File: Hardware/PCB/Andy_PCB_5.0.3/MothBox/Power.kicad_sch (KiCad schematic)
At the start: 42 parts, among them J1 DB141V-2.54-4P, J2 DB141V-2.54-4P, J3 DB141V-2.54-4P, Q1 JMTV210P02A, Q2 AO3400A, Q8 JMTV210P02A, SW2 KH-6X6X5H-STM, U1 Place Holder voltage regulator, U2 XL4015E1, U3 INA219BIDCNT

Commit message: version 5.0.3 completed changes, as per CHANGELOG
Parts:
- added D2, D4: 6.8V, MothBox_footprints_Library:D_SOD-323, symbol MothBox_Symbol_Library:D_Zener_Small
- added JP2: Jumper_2_Small_Bridged, symbol Jumper:Jumper_2_Small_Bridged
- added Q10: JMTV210P02A, MothBox_footprints_Library:U-DFN2020-6_L2.0-W2.0-P0.65-BL, symbol MothBox_Symbol_Library:JMTV210P02A
- added R38, R40, R41: 4.7K, MothBox_footprints_Library:R_0603_1608Metric, symbol MothBox_Symbol_Library:R_Small
- added R39: 10K, MothBox_footprints_Library:R_0603_1608Metric, symbol MothBox_Symbol_Library:R_Small
- D1: value 10V -> 6.8V; DESCRIPTION (none) -> BZT52C6V8S; LCSC_Part C571388 -> C46641604
- F2: value 6A trip -> 7A trip; footprint Fuse:Fuse_1812_4532Metric -> Fuse:Fuse_2920_7451Metric; LCSC_Part C7500481 -> C22363536
- R4: value 0.1R/1% -> 0.033R/1%; LCSC_Part C23067426 -> C875726
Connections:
- net +12V: now also D2.1 (K), Q10.4 (S), Q10.7 (S); no longer J1.3 (Pin_3), J1.4 (Pin_4), U1.4 (Vout+)
- net +24V: now also D4.1 (K), JP2.2 (B); no longer R30.1
- net GND: now also R38.2, R40.2, R41.1; no longer R29.2
- net at F2.2, R4.2, U3.1 (IN+): now also JP2.1 (A)
- net at Q2.3 (D), Q8.3 (G): no longer R30.2
- new net: R39.2, R40.1
- new net: R29.2, R38.1
- new net: D4.2 (A), R30.2
- new net: D2.2 (A), Q10.3 (G), R39.1
- new net: J1.3 (Pin_3), J1.4 (Pin_4), Q10.1 (D), Q10.2 (D), Q10.5 (D), Q10.6 (D), Q10.8 (D), U1.4 (Vout+)
- new net: R30.1, R41.2
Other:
- note added: "2920 size"
- note added: "Cut Jumper to measure current flow"
- note added: "INA219 Current Sensor Bypass"
- note added: "Switch the External Regulator on and Off"
- note added: "To External 12V Regulator"
- note removed: "Switch the Regulator on and Off"
- moved on the sheet: D1, J1, Q2, R1, R29, R30, TP5

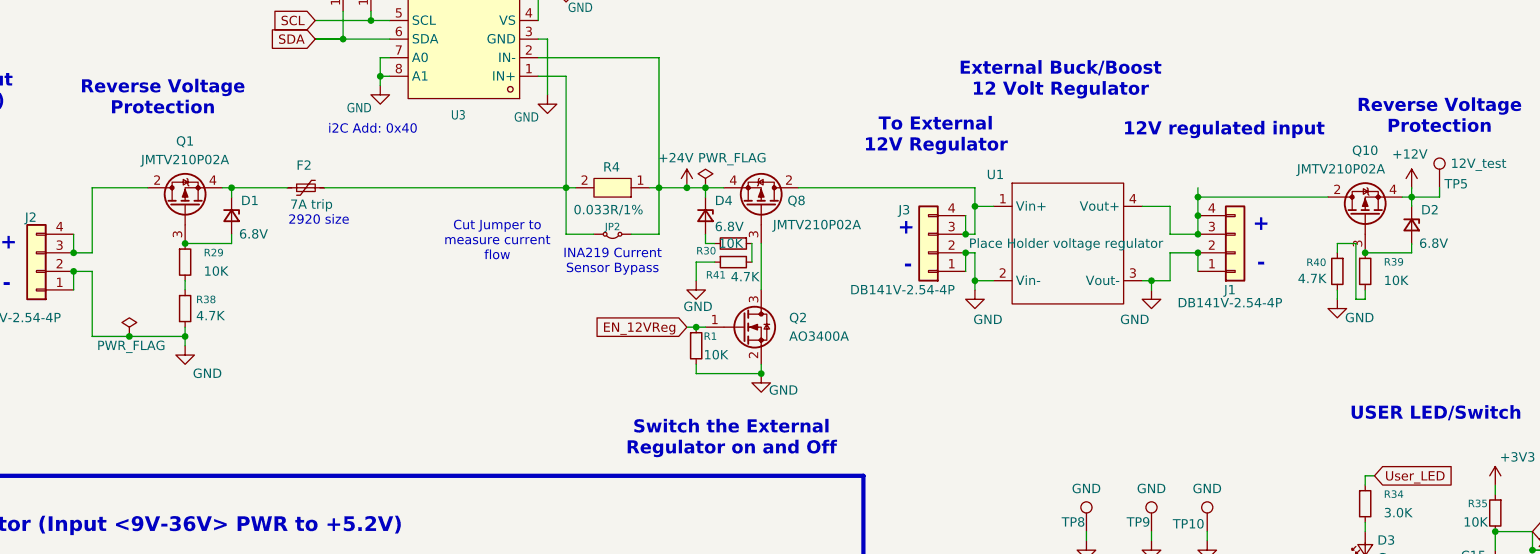
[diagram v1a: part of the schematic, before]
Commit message: swapped out Q1, Q8, Q10 for better specc'ed MOSFETs. Moved a few tracks around and updated CHANGELOG.txt
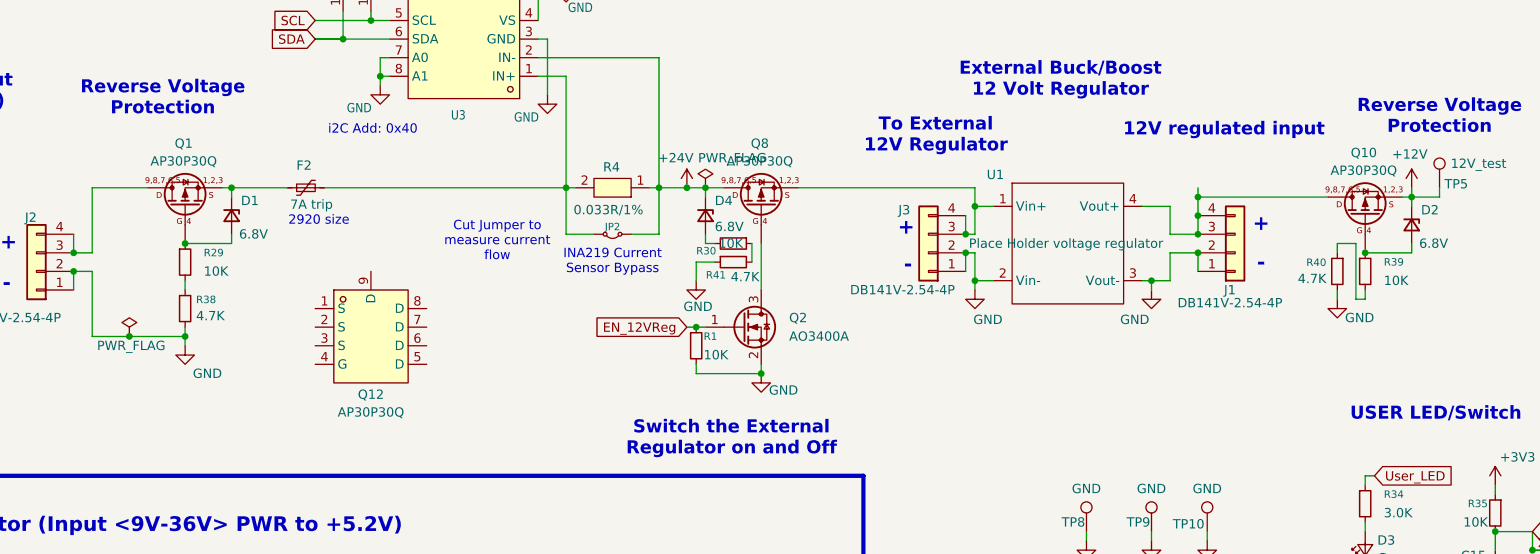
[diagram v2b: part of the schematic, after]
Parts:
- removed Q1, Q10, Q8: JMTV210P02A, MothBox_footprints_Library:U-DFN2020-6_L2.0-W2.0-P0.65-BL, symbol MothBox_Symbol_Library:JMTV210P02A
- added Q1, Q10, Q8: AP30P30Q, 0_easyeda_footprints:PDFN3333-8_L3.1-W3.2-P0.65-LS3.4-BL, symbol MothBox_Symbol_Library:AP30P30Q_1
- added Q12: AP30P30Q, easyeda2kicad:PDFN3333-8_L3.1-W3.2-P0.65-LS3.4-BL, symbol MothBox_Symbol_Library:AP30P30Q
- D3: symbol 0_pauls_symbols:Device_LED_Small -> MothBox_Symbol_Library:Device_LED_Small
- JP2: symbol Jumper:Jumper_2_Small_Bridged -> MothBox_Symbol_Library:Jumper_2_Small_Bridged
- Q2: symbol Transistor_FET:AO3400A -> MothBox_Symbol_Library:AO3400A
- SW2: symbol 0_easyeda2kicad:KH-6X6X5H-STM -> MothBox_Symbol_Library:KH-6X6X5H-STM
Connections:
- net +12V: now also Q10.1 (S), Q10.2 (S), Q10.3 (S)
- net +24V: now also Q8.5 (D), Q8.6 (D), Q8.7 (D), Q8.8 (D), Q8.9 (D)
- net at J3.3 (Pin_3), J3.4 (Pin_4), U1.1 (Vin+): now also Q8.1 (S), Q8.2 (S), Q8.3 (S)
- net at D1.1 (K), F2.1: now also Q1.1 (S), Q1.2 (S), Q1.3 (S)
- net at J2.3 (Pin_3), J2.4 (Pin_4): now also Q1.5 (D), Q1.6 (D), Q1.7 (D), Q1.8 (D), Q1.9 (D)
- net at D2.2 (A), R39.1: now also Q10.4 (G)
- net at D1.2 (A), R29.1: now also Q1.4 (G)
- net at J1.3 (Pin_3), J1.4 (Pin_4), U1.4 (Vout+): now also Q10.5 (D), Q10.6 (D), Q10.7 (D), Q10.8 (D), Q10.9 (D)
- net at Q2.3 (D): now also Q8.4 (G)

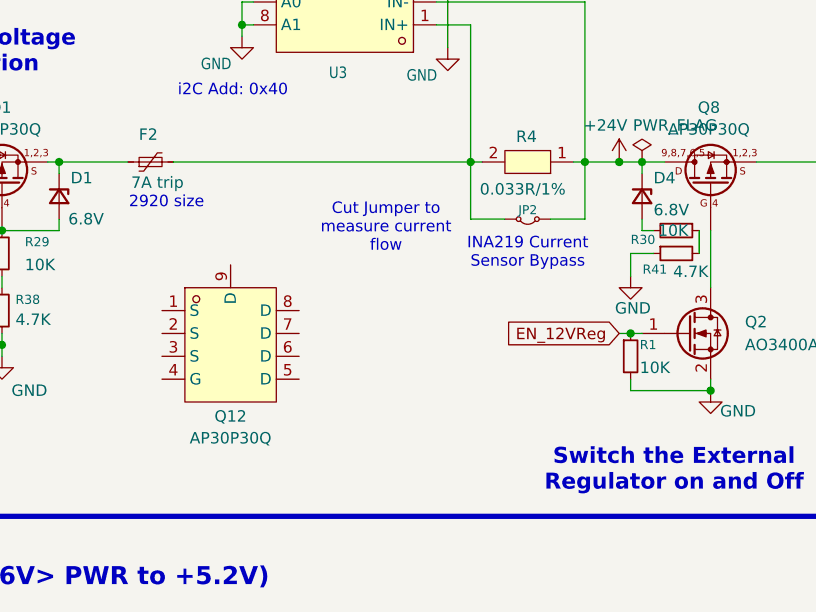
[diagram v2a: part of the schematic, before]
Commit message: Passes DRC - updated cuttable jumper, updated 3v3 mosfet, updated holes for battery
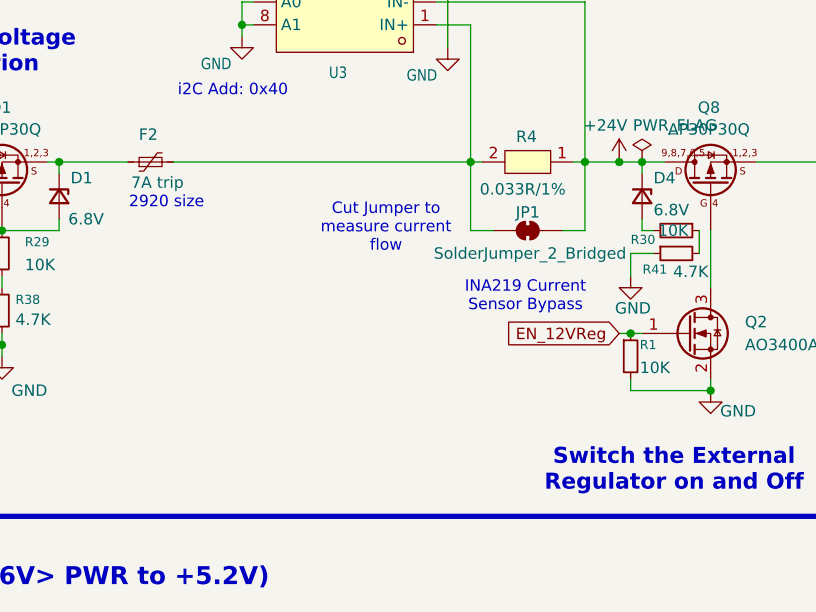
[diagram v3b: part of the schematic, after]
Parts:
- removed JP2: Jumper_2_Small_Bridged, symbol MothBox_Symbol_Library:Jumper_2_Small_Bridged
- removed Q12: AP30P30Q, easyeda2kicad:PDFN3333-8_L3.1-W3.2-P0.65-LS3.4-BL, symbol MothBox_Symbol_Library:AP30P30Q
- added JP1: SolderJumper_2_Bridged, Jumper:SolderJumper-2_P1.3mm_Bridged2Bar_RoundedPad1.0x1.5mm, symbol Jumper:SolderJumper_2_Bridged
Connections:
- net +24V: now also JP1.2 (B)
- net at F2.2, R4.2, U3.1 (IN+): now also JP1.1 (A)
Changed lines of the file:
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@@
 	(text "INA219 Current\nSensor Bypass"
 		(exclude_from_sim no)
-		(at 137.16 85.09 0)
+		(at 136.906 89.916 0)
 		(effects
 			(font
@@
 	(wire
 		(pts
+			(xy 133.35 82.55) (xy 130.81 82.55)
+		)
+		(stroke
+			(width 0)
+			(type default)
+		)
+	)
+	(wire
+		(pts
 			(xy 151.13 137.16) (xy 151.13 138.43)
 		)
@@
 	(wire
 		(pts
-			(xy 130.81 81.28) (xy 130.81 74.93)
+			(xy 130.81 82.55) (xy 130.81 74.93)
 		)
 		(stroke
@@
 	(wire
 		(pts
-			(xy 143.51 81.28) (xy 143.51 74.93)
+			(xy 143.51 82.55) (xy 143.51 74.93)
 		)
 		(stroke
@@
 	(wire
 		(pts
-			(xy 240.03 88.9) (xy 240.03 90.17)
+			(xy 140.97 82.55) (xy 143.51 82.55)
 		)
 		(stroke
@@
 	(wire
 		(pts
-			(xy 257.81 121.92) (xy 257.81 124.46)
+			(xy 240.03 88.9) (xy 240.03 90.17)
 		)
 		(stroke
@@
 	(wire
 		(pts
-			(xy 100.33 138.43) (xy 106.68 138.43)
+			(xy 257.81 121.92) (xy 257.81 124.46)
 		)
 		(stroke
@@
 	(wire
 		(pts
-			(xy 134.62 152.4) (xy 134.62 157.48)
+			(xy 100.33 138.43) (xy 106.68 138.43)
 		)
 		(stroke
@@
 	(wire
 		(pts
-			(xy 154.94 143.51) (xy 154.94 138.43)
+			(xy 134.62 152.4) (xy 134.62 157.48)
 		)
 		(stroke
@@
 	(wire
 		(pts
-			(xy 154.94 152.4) (xy 147.32 152.4)
+			(xy 154.94 143.51) (xy 154.94 138.43)
 		)
 		(stroke
@@
 	(wire
 		(pts
-			(xy 262.89 124.46) (xy 273.05 124.46)
+			(xy 154.94 152.4) (xy 147.32 152.4)
 		)
 		(stroke
@@
 	(wire
 		(pts
-			(xy 139.7 81.28) (xy 143.51 81.28)
+			(xy 262.89 124.46) (xy 273.05 124.46)
 		)
 		(stroke
@@
 	(wire
 		(pts
-			(xy 134.62 81.28) (xy 130.81 81.28)
-		)
-		(stroke
-			(width 0)
-			(type default)
-		)
-	)
-	(wire
-		(pts
 			(xy 257.81 129.54) (xy 257.81 132.08)
 		)
@@
 	)
 	(symbol
-		(lib_id "MothBox_Symbol_Library:Jumper_2_Small_Bridged")
-		(at 137.16 81.28 0)
-		(mirror x)
-		(unit 1)
-		(exclude_from_sim no)
-		(in_bom yes)
-		(on_board yes)
-		(dnp no)
-		(property "Reference" "JP2"
-			(at 137.16 80.264 0)
-			(effects
-				(font
-					(size 1 1)
-				)
-			)
-		)
-		(property "Value" "Jumper_2_Small_Bridged"
-			(at 137.16 83.4428 0)
-			(effects
-				(font
-					(size 1.27 1.27)
-				)
-				(hide yes)
-			)
-		)
-		(property "Footprint" ""
-			(at 137.16 81.28 0)
-			(effects
-				(font
-					(size 1.27 1.27)
-				)
-				(hide yes)
-			)
-		)
-		(property "Datasheet" "~"
-			(at 137.16 81.28 0)
-			(effects
-				(font
-					(size 1.27 1.27)
-				)
-				(hide yes)
-			)
-		)
-		(property "Description" "Jumper, 2-pole, small symbol, bridged"
-			(at 137.16 81.28 0)
-			(effects
-				(font
-					(size 1.27 1.27)
-				)
-				(hide yes)
-			)
-		)
-		(pin "2"
-		)
-		(pin "1"
-		)
-		(instances
-			(project ""
-				(path "/9021e528-fc76-4423-a3f3-30f5652071cc/4a573100-9946-48c2-8ae5-35f893607623"
-					(reference "JP2")
-					(unit 1)
-				)
-			)
-		)
-	)
-	(symbol
 		(lib_id "MothBox_Symbol_Library:GND")
 		(at 128.27 62.23 0)
@@
 	)
 	(symbol
+		(lib_id "Jumper:SolderJumper_2_Bridged")
+		(at 137.16 82.55 0)
+		(unit 1)
+		(exclude_from_sim no)
+		(in_bom no)
+		(on_board yes)
+		(dnp no)
+		(property "Reference" "JP1"
+			(at 137.16 80.518 0)
+			(effects
+				(font
+					(size 1.27 1.27)
+				)
+			)
+		)
+		(property "Value" "SolderJumper_2_Bridged"
+			(at 137.414 85.09 0)
+			(effects
+				(font
+					(size 1.27 1.27)
+				)
+			)
+		)
+		(property "Footprint" "Jumper:SolderJumper-2_P1.3mm_Bridged2Bar_RoundedPad1.0x1.5mm"
+			(at 137.16 82.55 0)
+			(effects
+				(font
+					(size 1.27 1.27)
+				)
+				(hide yes)
+			)
+		)
+		(property "Datasheet" "~"
+			(at 137.16 82.55 0)
+			(effects
+				(font
+					(size 1.27 1.27)
+				)
+				(hide yes)
+			)
+		)
+		(property "Description" "Solder Jumper, 2-pole, closed/bridged"
+			(at 137.16 82.55 0)
+			(effects
+				(font
+					(size 1.27 1.27)
+				)
+				(hide yes)
+			)
+		)
+		(pin "1"
+		)
+		(pin "2"
+		)
+		(instances
+			(project ""
+				(path "/9021e528-fc76-4423-a3f3-30f5652071cc/4a573100-9946-48c2-8ae5-35f893607623"
+					(reference "JP1")
+					(unit 1)
+				)
+			)
+		)
+	)
+	(symbol
 		(lib_id "MothBox_Symbol_Library:R_Small")
 		(at 78.74 91.44 0)
@@
 					(unit 1)
 				)
-			)
-		)
-	)
-	(symbol
-		(lib_id "MothBox_Symbol_Library:AP30P30Q")
-		(at 104.14 95.25 0)
-		(unit 1)
-		(exclude_from_sim no)
-		(in_bom yes)
-		(on_board yes)
-		(dnp no)
-		(fields_autoplaced yes)
-		(property "Reference" "Q12"
-			(at 104.14 103.1931 0)
-			(effects
-				(font
-					(size 1.27 1.27)
-				)
-			)
-		)
-		(property "Value" "AP30P30Q"
-			(at 104.14 105.6174 0)
-			(effects
-				(font
-					(size 1.27 1.27)
-				)
-			)
-		)
-		(property "Footprint" "easyeda2kicad:PDFN3333-8_L3.1-W3.2-P0.65-LS3.4-BL"
-			(at 104.14 106.68 0)
-			(effects
-				(font
-					(size 1.27 1.27)
-				)
-				(hide yes)
-			)
-		)
-		(property "Datasheet" ""
-			(at 104.14 95.25 0)
-			(effects
-				(font
-					(size 1.27 1.27)
-				)
-				(hide yes)
-			)
-		)
-		(property "Description" ""
-			(at 104.14 95.25 0)
-			(effects
-				(font
-					(size 1.27 1.27)
-				)
-				(hide yes)
-			)
-		)
-		(property "LCSC Part" "C471913"
-			(at 104.14 109.22 0)
-			(effects
-				(font
-					(size 1.27 1.27)
-				)
-				(hide yes)
-			)
-		)
-		(pin "8"
-		)
-		(pin "6"
-		)
-		(pin "2"
-		)
-		(pin "7"
-		)
-		(pin "9"
-		)
-		(pin "4"
-		)
-		(pin "3"
-		)
-		(pin "1"
-		)
-		(pin "5"
-		)
-		(instances
-			(project ""
-				(path "/9021e528-fc76-4423-a3f3-30f5652071cc/4a573100-9946-48c2-8ae5-35f893607623"
-					(reference "Q12")
-					(unit 1)
-				)

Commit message: Fixed big capacitor library footprint
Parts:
- C14, C16: footprint 0_easyeda_footprints:CAP-TH_BD16.0-P7.50-D1.2-FD -> easyeda2kicad:CAP-TH_BD16.0-P7.50-D1.2-FD
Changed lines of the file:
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@@
 			)
 		)
-		(property "Footprint" "0_easyeda_footprints:CAP-TH_BD16.0-P7.50-D1.2-FD"
+		(property "Footprint" "easyeda2kicad:CAP-TH_BD16.0-P7.50-D1.2-FD"
 			(at 134.62 146.05 0)
 			(effects
@@
 			)
 		)
-		(property "Footprint" "0_easyeda_footprints:CAP-TH_BD16.0-P7.50-D1.2-FD"
+		(property "Footprint" "easyeda2kicad:CAP-TH_BD16.0-P7.50-D1.2-FD"
 			(at 49.53 143.51 0)
 			(effects
@@
 			)
 		)
-		(property "Datasheet" "https://lcsc.com/product-detail/Aluminum-Electrolytic-Capacitors-Leaded_1000uF-20-50V_C106656.html"
+		(property "Datasheet" "~"
 			(at 49.53 143.51 0)
 			(effects
@@
 			)
 		)
-		(property "Description" ""
+		(property "Description" "Polarized capacitor, small US symbol"
 			(at 49.53 143.51 0)
 			(effects

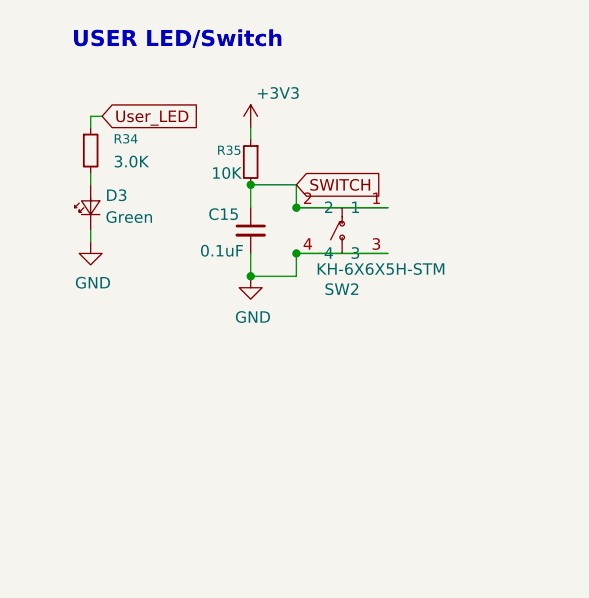
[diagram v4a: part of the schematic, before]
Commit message: Had to swap SW2 for a SMD version
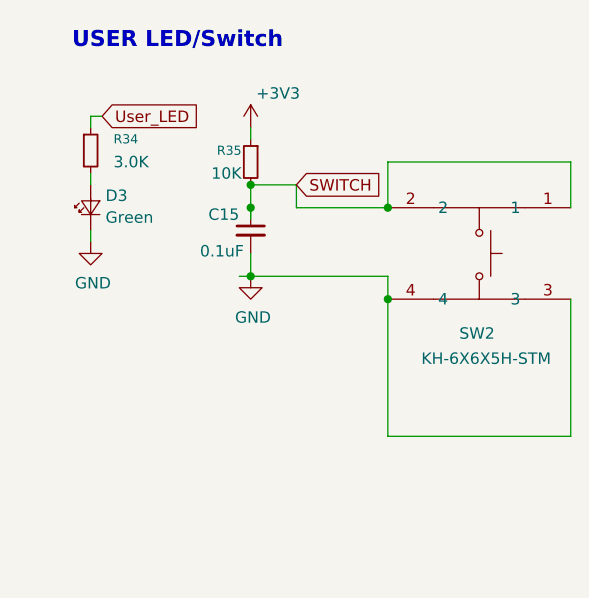
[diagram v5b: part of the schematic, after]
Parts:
- SW2: footprint 0_easyeda_footprints:SW-SMD_4P-L6.0-W6.0-P4.50-LS9.0_H5.0 -> easyeda2kicad:KEY-SMD_4P-L6.0-W6.0-P4.50-LS10.0-TL; symbol MothBox_Symbol_Library:KH-6X6X5H-STM -> easyeda2kicad:4-1437565-1; LCSC Part C455095 -> C592734
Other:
- moved on the sheet: SW2
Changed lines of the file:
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@@
 	)
 	(junction
+		(at 257.81 124.46)
+		(diameter 0)
+		(color 0 0 0 0)
+	)
+	(junction
 		(at 100.33 54.61)
 		(diameter 0)
@@
 	)
 	(junction
-		(at 186.69 87.63)
+		(at 273.05 134.62)
 		(diameter 0)
 		(color 0 0 0 0)
 	)
 	(junction
-		(at 63.5 86.36)
+		(at 186.69 87.63)
 		(diameter 0)
 		(color 0 0 0 0)
 	)
 	(junction
-		(at 134.62 138.43)
+		(at 63.5 86.36)
 		(diameter 0)
 		(color 0 0 0 0)
 	)
 	(junction
-		(at 154.94 138.43)
+		(at 134.62 138.43)
 		(diameter 0)
 		(color 0 0 0 0)
 	)
 	(junction
-		(at 262.89 124.46)
+		(at 154.94 138.43)
 		(diameter 0)
 		(color 0 0 0 0)
@@
 	)
 	(junction
-		(at 262.89 129.54)
-		(diameter 0)
-		(color 0 0 0 0)
-	)
-	(junction
 		(at 217.17 83.82)
 		(diameter 0)
@@
 	)
 	(junction
+		(at 273.05 124.46)
+		(diameter 0)
+		(color 0 0 0 0)
+	)
+	(junction
 		(at 185.42 81.28)
 		(diameter 0)
@@
 	(wire
 		(pts
+			(xy 293.37 119.38) (xy 273.05 119.38)
+		)
+		(stroke
+			(width 0)
+			(type default)
+		)
+	)
+	(wire
+		(pts
 			(xy 128.27 54.61) (xy 128.27 62.23)
 		)
@@
 	(wire
 		(pts
+			(xy 273.05 119.38) (xy 273.05 124.46)
+		)
+		(stroke
+			(width 0)
+			(type default)
+		)
+	)
+	(wire
+		(pts
 			(xy 104.14 52.07) (xy 96.52 52.07)
 		)
@@
 	(wire
 		(pts
-			(xy 262.89 129.54) (xy 273.05 129.54)
+			(xy 257.81 124.46) (xy 257.81 121.92)
 		)
 		(stroke
@@
 	(wire
 		(pts
-			(xy 262.89 129.54) (xy 262.89 132.08)
-		)
-		(stroke
-			(width 0)
-			(type default)
-		)
-	)
-	(wire
-		(pts
 			(xy 120.65 153.67) (xy 120.65 154.94)
 		)
@@
 	(wire
 		(pts
+			(xy 293.37 124.46) (xy 293.37 119.38)
+		)
+		(stroke
+			(width 0)
+			(type default)
+		)
+	)
+	(wire
+		(pts
 			(xy 149.86 82.55) (xy 149.86 81.28)
 		)
@@
 	(wire
 		(pts
+			(xy 256.54 132.08) (xy 257.81 132.08)
+		)
+		(stroke
+			(width 0)
+			(type default)
+		)
+	)
+	(wire
+		(pts
 			(xy 149.86 74.93) (xy 149.86 76.2)
 		)
@@
 	(wire
 		(pts
-			(xy 240.03 88.9) (xy 240.03 90.17)
+			(xy 273.05 132.08) (xy 273.05 134.62)
 		)
 		(stroke
@@
 	(wire
 		(pts
-			(xy 257.81 121.92) (xy 257.81 124.46)
+			(xy 240.03 88.9) (xy 240.03 90.17)
 		)
 		(stroke
@@
 	(wire
 		(pts
+			(xy 293.37 149.86) (xy 273.05 149.86)
+		)
+		(stroke
+			(width 0)
+			(type default)
+		)
+	)
+	(wire
+		(pts
 			(xy 134.62 152.4) (xy 134.62 157.48)
 		)
@@
 	(wire
 		(pts
+			(xy 273.05 149.86) (xy 273.05 134.62)
+		)
+		(stroke
+			(width 0)
+			(type default)
+		)
+	)
+	(wire
+		(pts
 			(xy 96.52 54.61) (xy 100.33 54.61)
 		)
@@
 	(wire
 		(pts
+			(xy 257.81 125.73) (xy 257.81 124.46)
+		)
+		(stroke
+			(width 0)
+			(type default)
+		)
+	)
+	(wire
+		(pts
 			(xy 88.9 149.86) (xy 96.52 149.86)
 		)
@@
 	(wire
 		(pts
+			(xy 293.37 134.62) (xy 293.37 149.86)
+		)
+		(stroke
+			(width 0)
+			(type default)
+		)
+	)
+	(wire
+		(pts
 			(xy 240.03 127) (xy 240.03 128.27)
 		)
@@
 	(wire
 		(pts
-			(xy 257.81 132.08) (xy 262.89 132.08)
+			(xy 257.81 132.08) (xy 273.05 132.08)
 		)
 		(stroke
@@
 	)
 	(symbol
-		(lib_id "MothBox_Symbol_Library:KH-6X6X5H-STM")
-		(at 267.97 127 0)
+		(lib_id "easyeda2kicad:4-1437565-1")
+		(at 283.21 129.54 0)
 		(mirror y)
 		(unit 1)
@@
 		(dnp no)
 		(property "Reference" "SW2"
-			(at 267.97 133.5575 0)
+			(at 282.956 138.43 0)
 			(effects
 				(font
@@
 		)
 		(property "Value" "KH-6X6X5H-STM"
-			(at 272.288 131.318 0)
+			(at 283.972 141.224 0)
 			(effects
 				(font
@@
 			)
 		)
-		(property "Footprint" "0_easyeda_footprints:SW-SMD_4P-L6.0-W6.0-P4.50-LS9.0_H5.0"
-			(at 267.97 137.16 0)
+		(property "Footprint" "easyeda2kicad:KEY-SMD_4P-L6.0-W6.0-P4.50-LS10.0-TL"
+			(at 283.21 142.24 0)
 			(effects
 				(font
@@
 		)
 		(property "Datasheet" ""
-			(at 267.97 127 0)
+			(at 283.21 129.54 0)
 			(effects
 				(font
@@
 		)
 		(property "Description" ""
-			(at 267.97 127 0)
+			(at 283.21 129.54 0)
 			(effects
 				(font
@@
 			)
 		)
-		(property "LCSC Part" "C455095"
-			(at 267.97 139.7 0)
+		(property "LCSC Part" "C592734"
+			(at 283.21 144.78 0)
 			(effects
 				(font
